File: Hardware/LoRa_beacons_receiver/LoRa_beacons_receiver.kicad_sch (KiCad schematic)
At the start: 28 parts, among them J1 Conn_Coaxial, J2 USB_C_Receptacle_USB2.0_14P, J3 I2C_Display, SW1 RST_button, SW2 BOOT_button, U1 LoRa-E5, U2 CP2102N-Axx-xQFN28, U3 AP2112K-3.3

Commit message: First complete schematic version
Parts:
- removed J2: USB_C_Receptacle_USB2.0_14P, symbol Connector:USB_C_Receptacle_USB2.0_14P
- removed U1: LoRa-E5, symbol STM32WLE5JC:LoRa-E5
- added D4: 1PPS, LED_SMD:LED_0805_2012Metric_Pad1.15x1.40mm_HandSolder, symbol Device:LED
- added J2: USB_C_Receptacle_USB2.0_16P, Connector_USB:USB_C_Receptacle_GCT_USB4105-xx-A_16P_TopMnt_Horizontal, symbol Connector:USB_C_Receptacle_USB2.0_16P
- added J4: ST-Link, Connector_PinSocket_2.54mm:PinSocket_1x04_P2.54mm_Horizontal, symbol Connector:Conn_01x04_Socket
- added J5: 1PPS_out, Connector_PinSocket_2.54mm:PinSocket_1x02_P2.54mm_Horizontal, symbol Connector:Conn_01x02_Socket
- added J6, J7: Conn_01x09_Socket, Connector_PinSocket_2.54mm:PinSocket_1x09_P2.54mm_Vertical, symbol Connector:Conn_01x09_Socket
- added Q1, Q2: DMG3402L, Package_TO_SOT_SMD:SOT-23, symbol Transistor_FET:DMG3402L
- added R8: 56R, Resistor_SMD:R_0805_2012Metric_Pad1.20x1.40mm_HandSolder, symbol Device:R
- added U1: STM32WLE5JC, STM32_module_l:STM32WLE5JC, symbol STM32_module_l:STM32WLE5JC
- C1, C2, C3, C4, C5, C6, C7, C8, C9: footprint (none) -> Capacitor_SMD:C_0805_2012Metric_Pad1.18x1.45mm_HandSolder
- D2: footprint (none) -> LED_SMD:LED_0805_2012Metric_Pad1.15x1.40mm_HandSolder
- D3: footprint (none) -> Diode_SMD_l:SOD-123FL
- F1: footprint (none) -> Fuse:Fuse_0805_2012Metric_Pad1.15x1.40mm_HandSolder
- J1: footprint (none) -> Connector_Coaxial:SMA_Molex_73251-1153_EdgeMount_Horizontal
- J3: footprint (none) -> Connector_PinSocket_2.54mm:PinSocket_1x04_P2.54mm_Vertical
- R1, R2, R3, R4, R5, R6, R7: footprint (none) -> Resistor_SMD:R_0805_2012Metric_Pad1.20x1.40mm_HandSolder
- SW1, SW2: footprint (none) -> Button_Switch_THT:SW_PUSH_6mm
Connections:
- net +3.3V: now also D4.2 (A), J4.1 (Pin_1), J5.1 (Pin_1), J6.2 (Pin_2), U1.1 (VCC)
- net +5V: now also J6.1 (Pin_1)
- net CC1: now also J2.A5 (CC1)
- net CC2: now also J2.B5 (CC2)
- net D+: now also J2.A6 (D+), J2.B6 (D+)
- net D-: now also J2.A7 (D-), J2.B7 (D-)
- net GND: now also J2.A1 (GND), J2.A12 (GND), J2.B1 (GND), J2.B12 (GND), J2.S1 (SHIELD), J4.2 (Pin_2), J6.3 (Pin_3), J7.9 (Pin_9), Q1.2 (S), Q2.2 (S), U1.14 (GND), U1.16 (GND), U1.2 (GND), U1.22 (GND)
- net I2C2_SCL: now also J7.1 (Pin_1), U1.5 (PB15)
- net I2C2_SDA: now also J7.2 (Pin_2), U1.6 (PA15)
- net LPUART1_RX: now also J6.9 (Pin_9), U1.13 (PC0)
- net LPUART1_TX: now also J6.8 (Pin_8), U1.12 (PC1)
- net RFIO: now also U1.15 (RFIO)
- net RST: now also U1.17 (RST)
- net SPI2_MISO: now also J7.7 (Pin_7), U1.26 (PB14)
- net SPI2_MOSI: now also J7.8 (Pin_8), U1.27 (PA10)
- net SPI2_NSS: now also J7.6 (Pin_6), U1.25 (PB9)
- net SPI2_SCK;BOOT: now also J7.5 (Pin_5), U1.24 (PB13~{})
- net SWCLK: now also J4.4 (Pin_4), U1.4 (PA14)
- net SWDIO: now also J4.3 (Pin_3), U1.3 (PA13)
- net UART1_RX-USB: now also U1.10 (PB6)
- net UART1_TX-USB: now also U1.9 (PB7)
- net UART2_RX: now also J7.3 (Pin_3), U1.18 (PA3)
- net UART2_TX: now also J7.4 (Pin_4), U1.19 (PA2)
- net VBUS: now also J2.A4 (VBUS), J2.A9 (VBUS), J2.B4 (VBUS), J2.B9 (VBUS)
- new net 1PPS_LED: Q2.1 (G), U1.8 (PB3)
- new net 1PPS_OUT: Q1.1 (G), U1.23 (PA0)
- new net PA9: J6.7 (Pin_7), U1.21 (PA9)
- new net PB10: J6.6 (Pin_6), U1.20 (PB10)
- new net PB4: J6.4 (Pin_4), U1.7 (PB4)
- new net PB5: J6.5 (Pin_5), U1.11 (PB5)
- new net PPS_LED: D4.1 (K), R8.1
- new net PPS_LED_MOS_D: Q2.3 (D), R8.2
- new net PPS_OUT_MOS_D: J5.2 (Pin_2), Q1.3 (D)
- no-connect marks 18 -> 20
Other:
- note added: "1PPS output"
- note added: "Connectors"
- moved on the sheet: C1, C2, C3, C4, C5, C6, C7, C8, C9, D1, D2, D3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

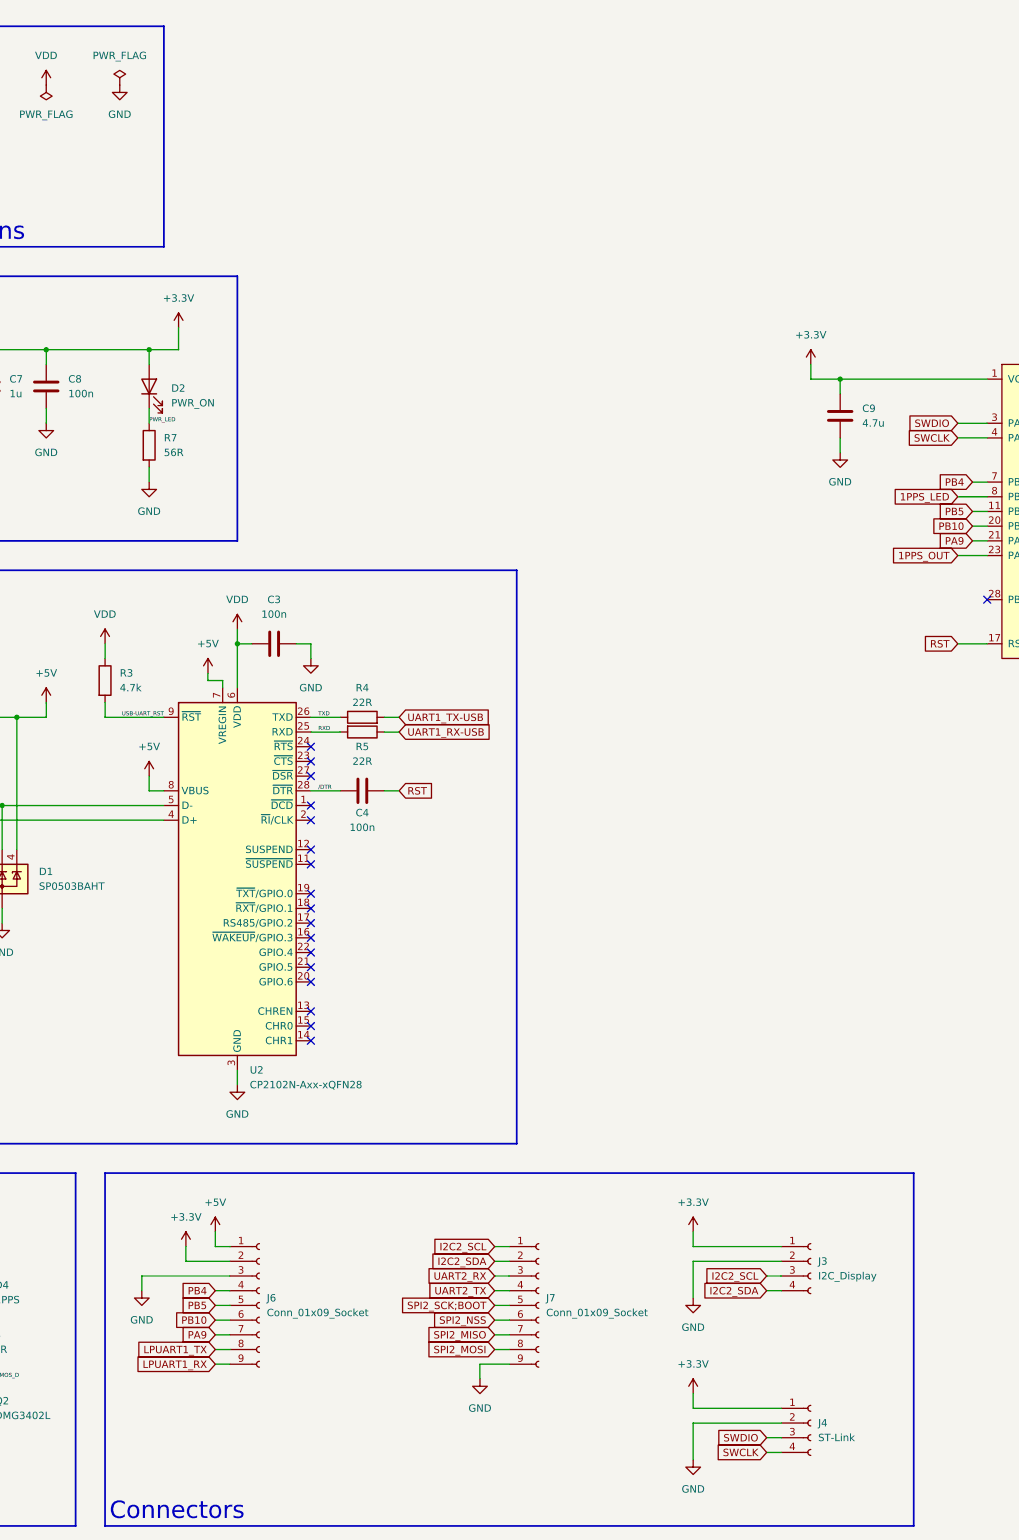
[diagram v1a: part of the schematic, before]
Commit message: Minor schematic adjustments; first version of PCB layout
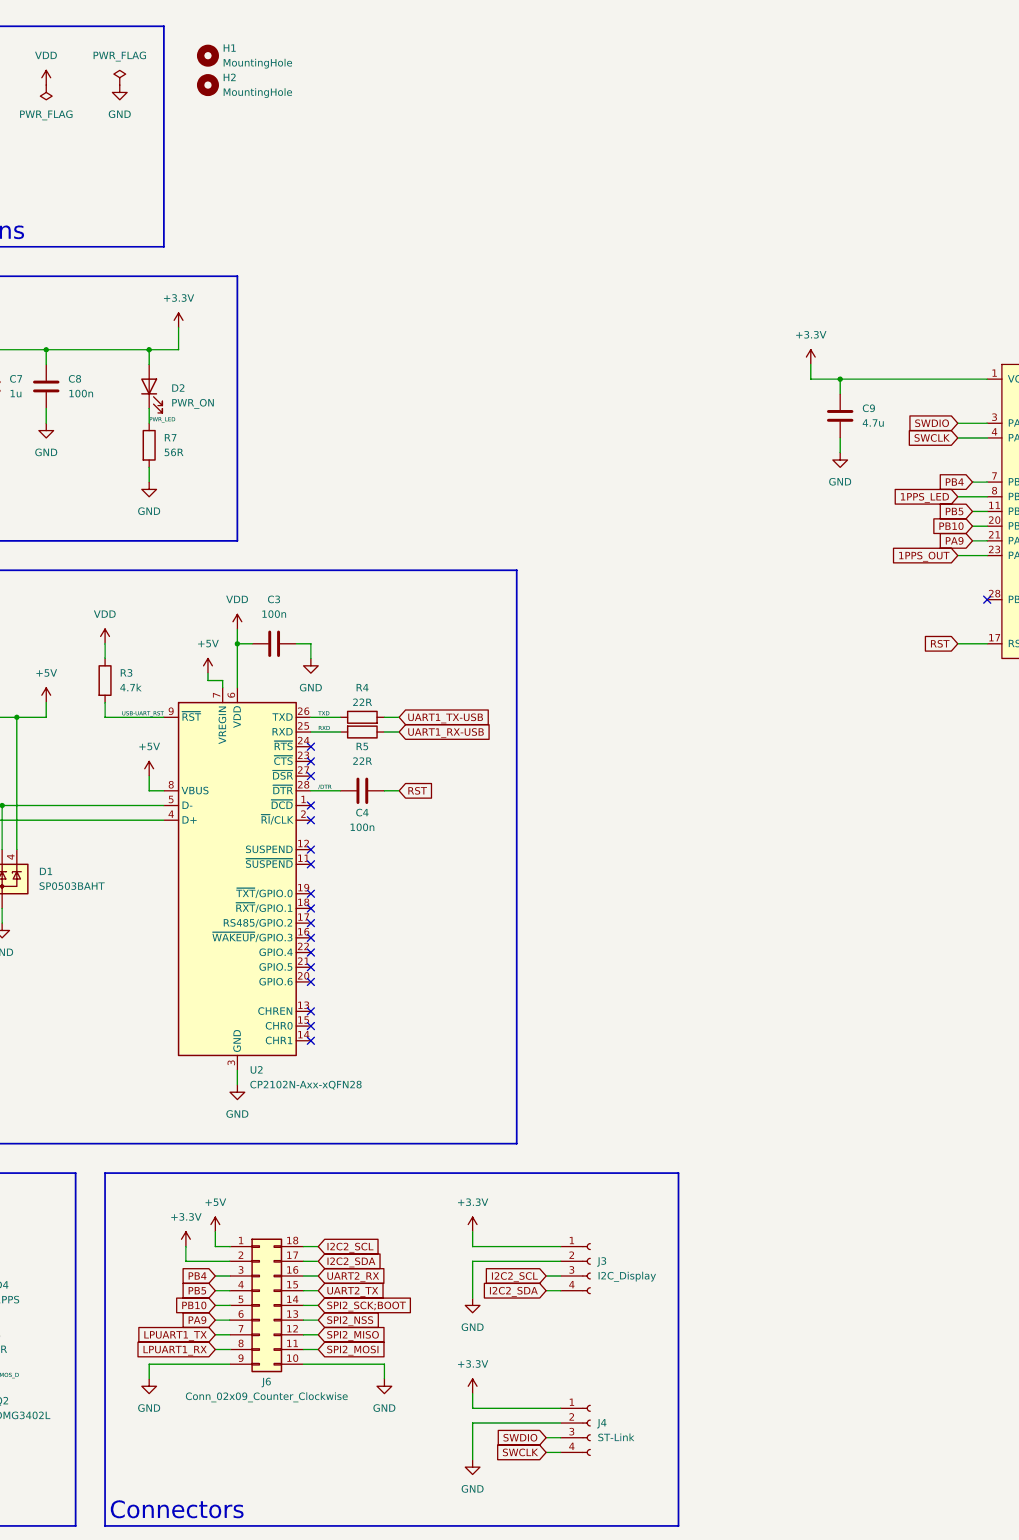
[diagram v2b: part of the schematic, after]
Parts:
- removed J6, J7: Conn_01x09_Socket, Connector_PinSocket_2.54mm:PinSocket_1x09_P2.54mm_Vertical, symbol Connector:Conn_01x09_Socket
- added H1, H2: MountingHole, MountingHole:MountingHole_2.2mm_M2, symbol Mechanical:MountingHole
- added J6: Conn_02x09_Counter_Clockwise, Connector_PinSocket_2.54mm:PinSocket_2x09_P2.54mm_Vertical, symbol Connector_Generic:Conn_02x09_Counter_Clockwise
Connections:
- net +3.3V: now also J6.2 (Pin_2)
- net +5V: now also J6.1 (Pin_1)
- net GND: now also J6.10 (Pin_10), J6.9 (Pin_9)
- net I2C2_SCL: now also J6.18 (Pin_18)
- net I2C2_SDA: now also J6.17 (Pin_17)
- net LPUART1_RX: now also J6.8 (Pin_8)
- net LPUART1_TX: now also J6.7 (Pin_7)
- net PA9: now also J6.6 (Pin_6)
- net PB10: now also J6.5 (Pin_5)
- net PB4: now also J6.3 (Pin_3)
- net PB5: now also J6.4 (Pin_4)
- net SPI2_MISO: now also J6.12 (Pin_12)
- net SPI2_MOSI: now also J6.11 (Pin_11)
- net SPI2_NSS: now also J6.13 (Pin_13)
- net SPI2_SCK;BOOT: now also J6.14 (Pin_14)
- net UART2_RX: now also J6.16 (Pin_16)
- net UART2_TX: now also J6.15 (Pin_15)
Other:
- moved on the sheet: J3, J4

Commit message: Recommended KiCAD changes; PCB layout changes
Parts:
- removed J4: ST-Link, Connector_PinSocket_2.54mm:PinSocket_1x04_P2.54mm_Horizontal, symbol Connector:Conn_01x04_Socket
- removed Q1, Q2: DMG3402L, Package_TO_SOT_SMD:SOT-23, symbol Transistor_FET:DMG3402L
- added C4: 100n, Capacitor_SMD:C_0805_2012Metric_Pad1.18x1.45mm_HandSolder, symbol Device:C
- added D5: PB4, LED_SMD:LED_0805_2012Metric_Pad1.15x1.40mm_HandSolder, symbol Device:LED
- added D6: PB5, LED_SMD:LED_0805_2012Metric_Pad1.15x1.40mm_HandSolder, symbol Device:LED
- added H3, H4: MountingHole, MountingHole:MountingHole_2.2mm_M2, symbol Mechanical:MountingHole
- added J4: ST-Link, Connector_PinSocket_2.54mm:PinSocket_1x05_P2.54mm_Vertical, symbol Connector:Conn_01x05_Socket
- added R10, R9: 56R, Resistor_SMD:R_0805_2012Metric_Pad1.20x1.40mm_HandSolder, symbol Device:R
- added R11, R12: 4.7k, Resistor_SMD:R_0805_2012Metric_Pad1.20x1.40mm_HandSolder, symbol Device:R
- added U4: 74LVC1G175, Package_TO_SOT_SMD:SOT-23-6_Handsoldering, symbol 74xGxx:74LVC1G175
- C1: renamed from C3; value 100n -> 4.7u
- J1: footprint Connector_Coaxial:SMA_Molex_73251-1153_EdgeMount_Horizontal -> Connector_Coaxial_g:RF2-143-T-17-50-G
- renumbered C4 to C10, C1 to C2, C2 to C3
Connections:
- net PPS_OUT_MOS_D is gone; now on net GND: J5.2 (Pin_2)
- net USB-UART_RST is gone; now on net /RST: R3.2, U2.9 (~{RST})
- net +3.3V: now also C1.2, C2.1, C3.1, R3.1, R7.1, U2.6 (VDD), U2.7 (VREGIN), C4.1, J4.1 (Pin_1), R11.2, R12.2, U4.3 (D), U4.5 (VCC); no longer D2.2 (A), D4.2 (A), J5.1 (Pin_1)
- net +5V: no longer C2.1, C3.1, U2.7 (VREGIN)
- net 1PPS_LED: now also R8.1
- net GND: now also C1.1, D2.1 (K), D4.1 (K), C4.2, J4.2 (Pin_2), R10.2, R9.2, U4.2 (GND); no longer C1.2, R7.2
- net I2C2_SCL: now also R11.1
- net I2C2_SDA: now also R12.1
- net PB4: now also D5.2 (A)
- net PB5: now also D6.2 (A)
- net SWCLK: now also J4.4 (Pin_4)
- net SWDIO: now also J4.3 (Pin_3)
- net 1PPS_OUT renamed 1PPS_CLK
- net 1PPS_CLK: now also U4.1 (C)
- removed net PPS_LED: D4.1 (K), R8.1
- net PPS_LED_MOS_D renamed PPS_LED_A
- net PPS_LED_A: now also D4.2 (A)
- removed net PWR_LED: D2.1 (K), R7.1
- net RST renamed /RST
- net /RST: now also J4.5 (Pin_5), U4.6 (~{CLR})
- removed net VDD: C1.1, R3.1, U2.6 (VDD)
- new net PB4_LED_K: D5.1 (K), R9.1
- new net PB5_LED_K: D6.1 (K), R10.1
- new net PPS_OUT: J5.1 (Pin_1), U4.4 (Q)
- new net PWR_LED_A: D2.2 (A), R7.2
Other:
- note added: "I2C"
- note added: "Signalization"
- moved on the sheet: C1, C10, C2, C3, C5, C6, C7, C8, C9, D1, D2, D3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

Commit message: Clenaup
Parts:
- J1: footprint Connector_Coaxial_g:RF2-143-T-17-50-G -> Connector_Coaxial_l:RF2-143-T-17-50-G_l
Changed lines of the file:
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@@
 			)
 		)
-		(property "Footprint" "Connector_Coaxial_g:RF2-143-T-17-50-G"
+		(property "Footprint" "Connector_Coaxial_l:RF2-143-T-17-50-G_l"
 			(at 320.04 45.72 0)
 			(effects
